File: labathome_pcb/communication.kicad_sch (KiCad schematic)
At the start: 18 parts, among them M1 W5500_mini, SW2 ON RS TERM, SW3 ON CAN TERM, U1 MAX3485, U15 NRF24L01, U6 RFM95W-868S2, U7 SN65HVD230, X3 SIM7080G

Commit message: Minor changes
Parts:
- C11, C3: MPN (none) -> GRM033R61A104KE15D; Manufacturer (none) -> Murata Electronics
- C59: MPN (none) -> CL05A105KA5NQNC; Manufacturer (none) -> Samsung Electro-Mechanics
- D2: MPN (none) -> PSM712; Manufacturer (none) -> TECH PUBLIC
- D3: MPN (none) -> NUP2105L; Manufacturer (none) -> TECH PUBLIC
- R20, R46: MPN (none) -> 1206W4F1200T5E; Manufacturer (none) -> UNI-ROYAL(Uniroyal Elec)
- R21: MPN (none) -> 0201WMF1002TEE; Manufacturer (none) -> UNI-ROYAL(Uniroyal Elec)
- R5, R8: MPN (none) -> 0402WGF1001TCE; Manufacturer (none) -> UNI-ROYAL(Uniroyal Elec)
- SW2, SW3: MPN (none) -> MSK12C02; Manufacturer (none) -> SHOU HAN
- U1: MPN (none) -> SP3485EEN(UMW); Manufacturer (none) -> UMW(Youtai Semiconductor Co., Ltd.)
- U7: MPN (none) -> SN65HVD230DR; Manufacturer (none) -> Texas Instruments

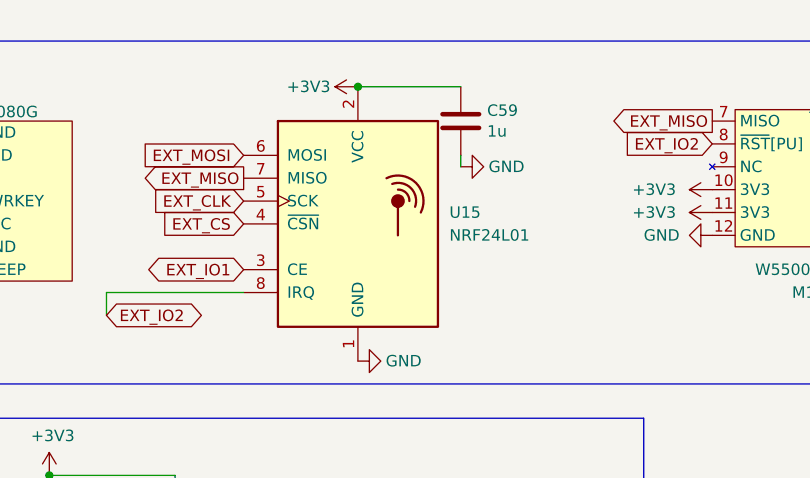
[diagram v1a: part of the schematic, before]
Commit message: Labathome PCB -> KICAD 9
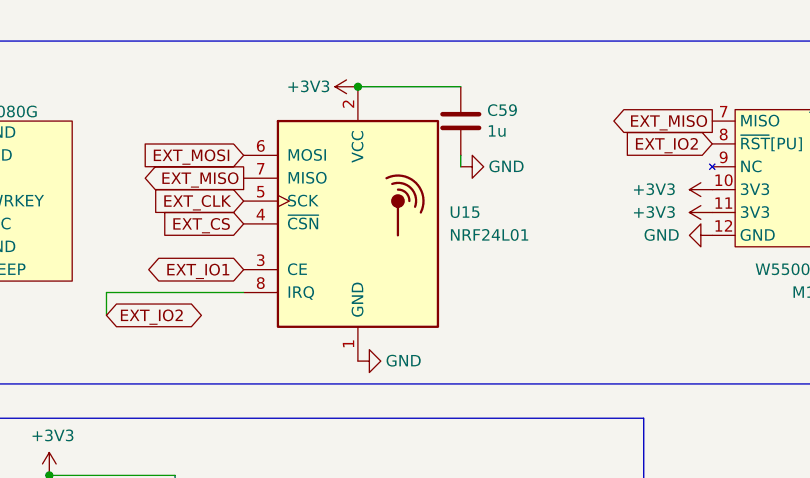
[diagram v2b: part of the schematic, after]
